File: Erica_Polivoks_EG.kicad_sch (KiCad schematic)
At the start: 92 parts, among them J1 GATE IN, J2 INV EG OUT, J3 Eurorack_Power_10pin_Unshroud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, J4 GATE DELAY OUT, J5 EG OUT, Q1 2N3904, Q2 2N3904, Q3 2N3904, Q4 2N3904, Q5 2N3904, Q6 2N3904, Q7 2N3906, Q8 2N3906, Q9 2N3906, SW1 SW_DPDT_x2, U1 TL074

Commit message: v1.1 ready for final check
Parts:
- R1, R2, R3: footprint Resistor_THT:R_Axial_DIN0207_L6.3mm_D2.5mm_P7.62mm_Horizontal -> Library:R_Axial_DIN0204_L3.6mm_D1.6mm_P7.62mm_Horizontal_Widened; Silkscreen Value (none) -> 200Ω
- R10, R11, R12, R13, R14, R15, R16, R17, R18, R19, R20, R21, R22, R23, R24, R25, R26, R27, R28, R29, R30, R31, R32, R33, R35, R36, R38, R39, R4, R40, R42, R43, R45, R47, R48, R49, R5, R50, R51, R6, R7, R8, R9: footprint Resistor_THT:R_Axial_DIN0207_L6.3mm_D2.5mm_P7.62mm_Horizontal -> Library:R_Axial_DIN0204_L3.6mm_D1.6mm_P7.62mm_Horizontal_Widened
- R34: value NU 39K -> NU 39k; footprint Resistor_THT:R_Axial_DIN0207_L6.3mm_D2.5mm_P7.62mm_Horizontal -> Library:R_Axial_DIN0204_L3.6mm_D1.6mm_P7.62mm_Horizontal_Widened
- R37, R44: footprint Resistor_THT:R_Axial_DIN0207_L6.3mm_D2.5mm_P7.62mm_Horizontal -> Library:R_Axial_DIN0204_L3.6mm_D1.6mm_P7.62mm_Horizontal_Widened; Silkscreen Value ◀470 -> ◀470Ω
- R41: footprint Resistor_THT:R_Axial_DIN0207_L6.3mm_D2.5mm_P7.62mm_Horizontal -> Library:R_Axial_DIN0204_L3.6mm_D1.6mm_P7.62mm_Horizontal_Widened; Silkscreen Value (none) -> 470Ω
- R46: footprint Resistor_THT:R_Axial_DIN0207_L6.3mm_D2.5mm_P7.62mm_Horizontal -> Library:R_Axial_DIN0204_L3.6mm_D1.6mm_P7.62mm_Horizontal_Widened; Silkscreen Value (none) -> 3.3k▼

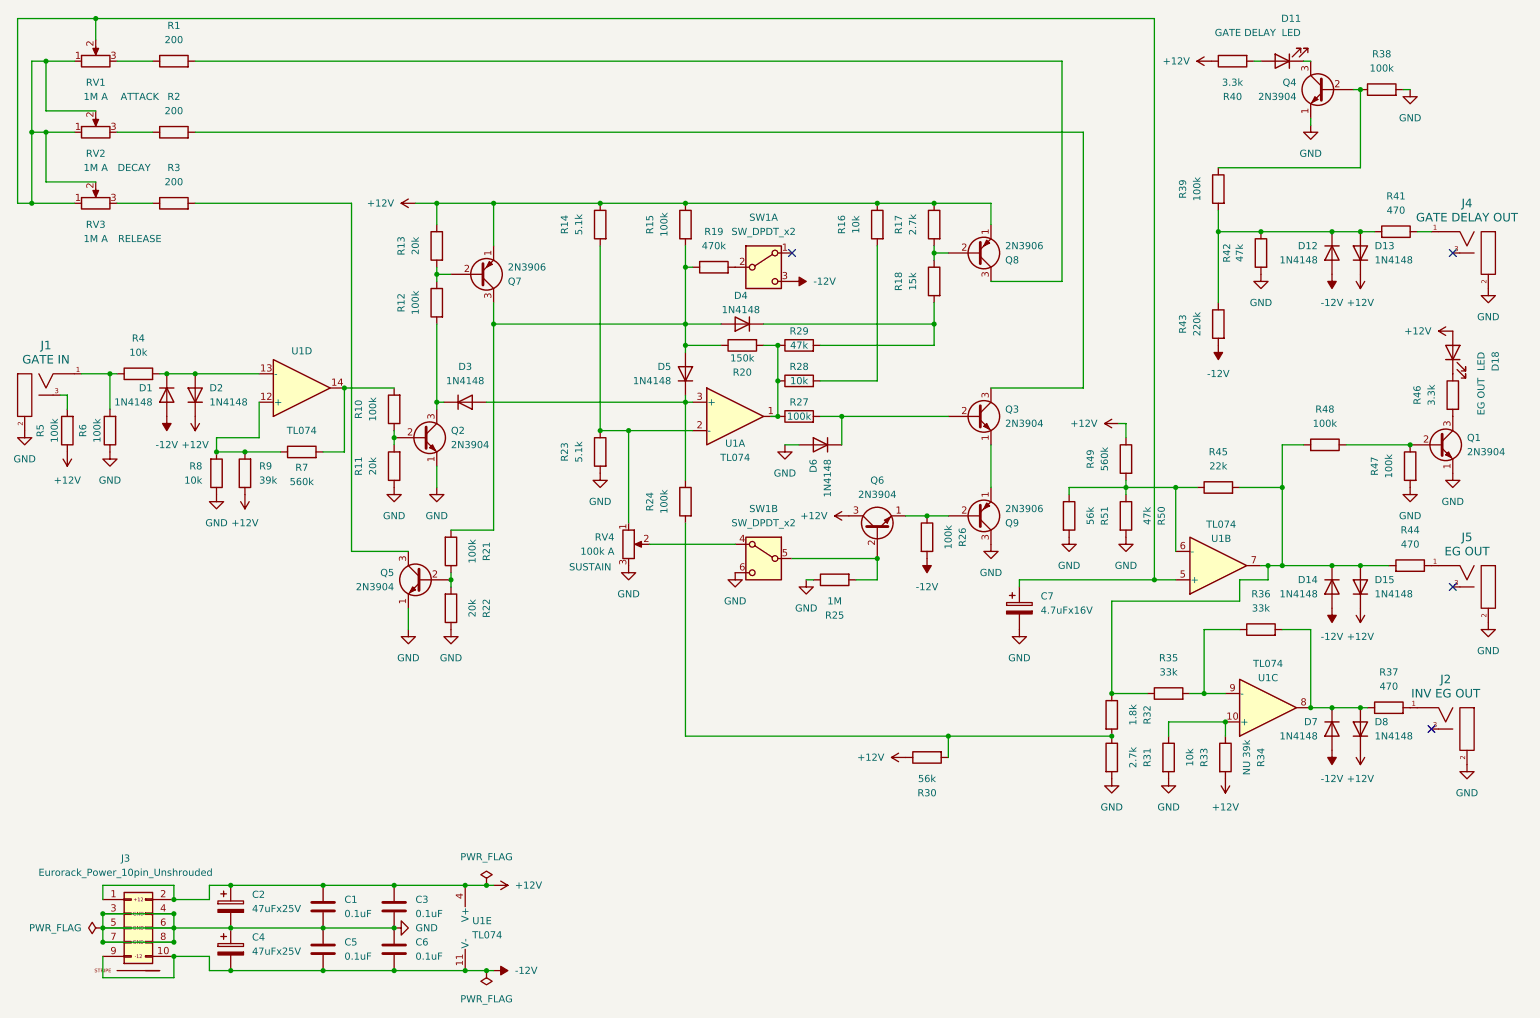
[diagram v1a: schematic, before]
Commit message: rerouting complete and passes DRC
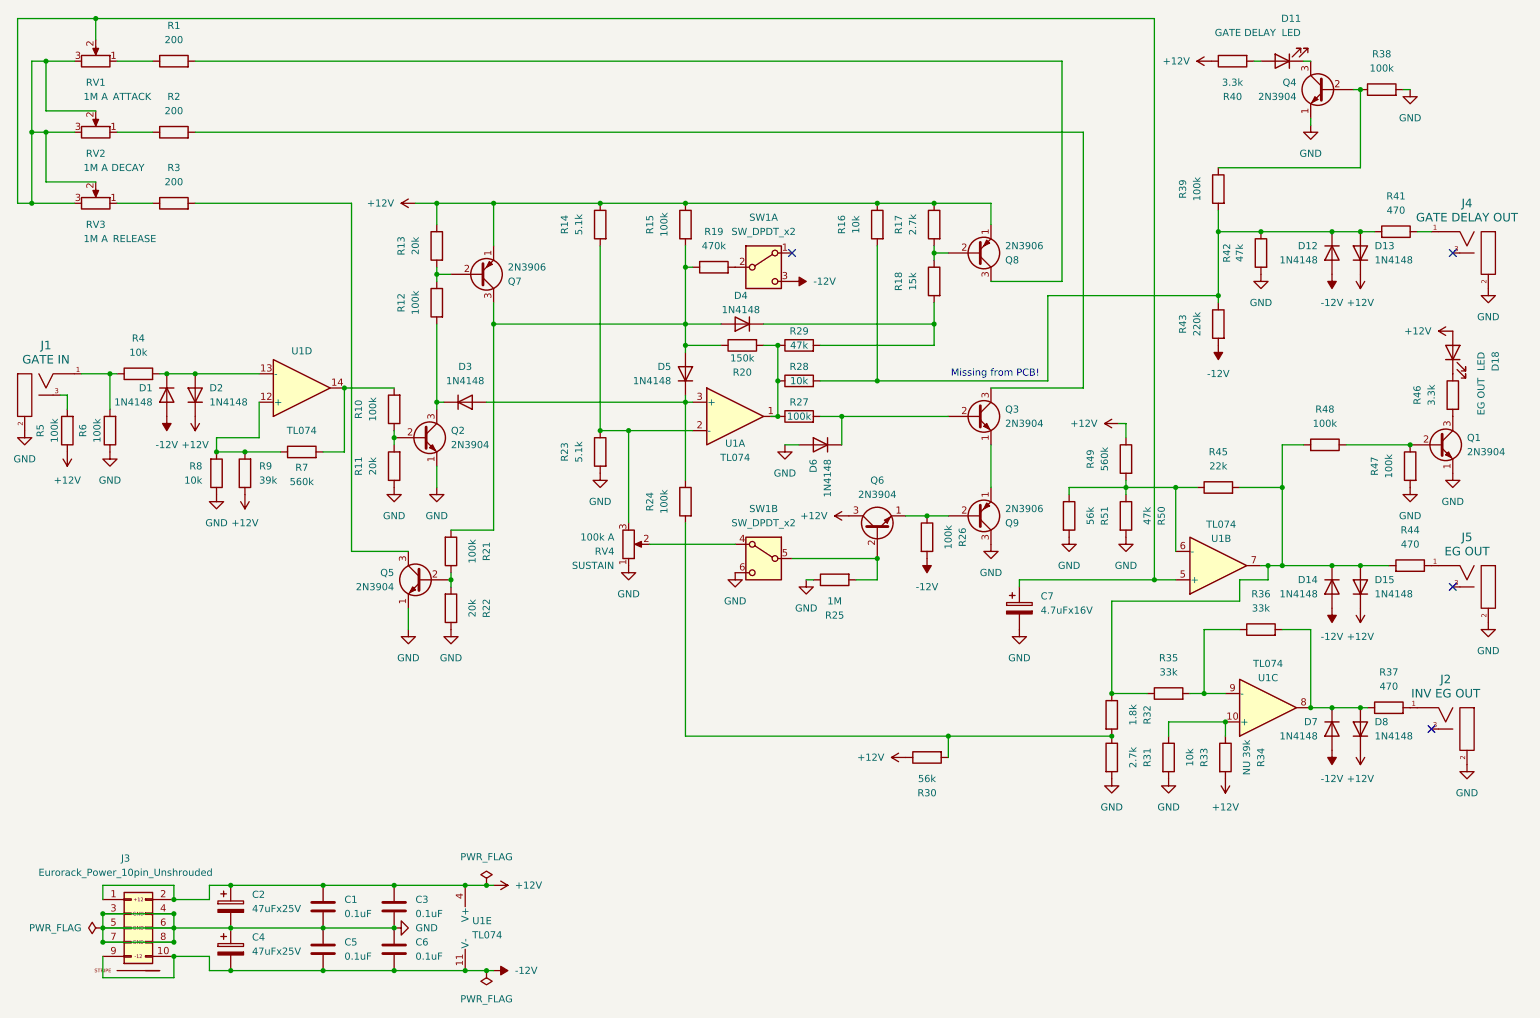
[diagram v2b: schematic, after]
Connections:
- net GND: now also RV4.1; no longer RV4.3
- net at R14.2, R23.1, U1.2 (-): now also RV4.3; no longer RV4.1
- net at C7.1, RV1.2, RV2.2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: now also RV1.3, RV2.3, RV3.3; no longer RV1.1, RV2.1, RV3.1
- net at D12.1 (K), D13.2 (A), R39.2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: now also R16.2, R28.2
- net at R1.1: now also RV1.1; no longer RV1.3
- net at R2.1: now also RV2.1; no longer RV2.3
- net at R3.1: now also RV3.1; no longer RV3.3
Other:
- note added: "Missing from PCB!"
- moved on the sheet: RV1, RV2, RV3
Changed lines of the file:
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@@
 	)
 	(junction
+		(at 229.87 67.31)
+		(diameter 0)
+		(color 0 0 0 0)
+	)
+	(junction
 		(at 255.27 115.57)
 		(diameter 0)
@@
 	)
 	(junction
+		(at 168.91 82.55)
+		(diameter 0)
+		(color 0 0 0 0)
+	)
+	(junction
 		(at 119.38 91.44)
 		(diameter 0)
@@
 	(wire
 		(pts
+			(xy 199.39 67.31) (xy 229.87 67.31)
+		)
+		(stroke
+			(width 0)
+			(type default)
+			(color 255 1 13 1)
+		)
+	)
+	(wire
+		(pts
 			(xy 29.21 17.78) (xy 29.21 21.59)
 		)
@@
 	(wire
 		(pts
-			(xy 229.87 55.88) (xy 229.87 68.58)
+			(xy 229.87 55.88) (xy 229.87 67.31)
 		)
 		(stroke
@@
 	(wire
 		(pts
+			(xy 168.91 82.55) (xy 199.39 82.55)
+		)
+		(stroke
+			(width 0)
+			(type default)
+			(color 255 1 13 1)
+		)
+	)
+	(wire
+		(pts
 			(xy 100.33 50.8) (xy 100.33 58.42)
 		)
@@
 	(wire
 		(pts
+			(xy 229.87 67.31) (xy 229.87 68.58)
+		)
+		(stroke
+			(width 0)
+			(type default)
+		)
+	)
+	(wire
+		(pts
 			(xy 152.4 93.98) (xy 154.94 93.98)
 		)
@@
 	(wire
 		(pts
+			(xy 199.39 82.55) (xy 199.39 67.31)
+		)
+		(stroke
+			(width 0)
+			(type default)
+			(color 255 1 13 1)
+		)
+	)
+	(wire
+		(pts
 			(xy 226.06 101.6) (xy 222.25 101.6)
 		)
@@
 		)
 	)
+	(text "Missing from PCB!"
+		(exclude_from_sim no)
+		(at 189.992 81.28 0)
+		(effects
+			(font
+				(size 1.27 1.27)
+			)
+		)
+	)
 	(symbol
 		(lib_id "Switch:SW_DPDT_x2")
@@
 	(symbol
 		(lib_id "Device:R_Potentiometer")
-		(at 29.21 38.1 90)
+		(at 29.21 38.1 270)
+		(mirror x)
 		(unit 1)
 		(exclude_from_sim no)
@@
 		)
 		(property "Description" "DECAY"
-			(at 36.068 44.45 90)
+			(at 32.004 44.45 90)
 			(effects
 				(font
 					(size 1.27 1.27)
 				)
+				(justify left)
 			)
 		)
@@
 		(lib_id "Device:R_Potentiometer")
 		(at 124.46 111.76 0)
+		(mirror x)
 		(unit 1)
 		(exclude_from_sim no)
@@
 		(dnp no)
 		(property "Reference" "RV4"
-			(at 121.92 110.4899 0)
+			(at 121.92 113.0301 0)
 			(effects
 				(font
@@
 		)
 		(property "Value" "100k A"
-			(at 121.92 113.0299 0)
+			(at 121.92 110.4901 0)
 			(effects
 				(font
@@
 		)
 		(property "Description" "SUSTAIN"
-			(at 117.602 115.824 0)
+			(at 118.11 115.57 0)
 			(effects
 				(font
@@
 	(symbol
 		(lib_id "Device:R_Potentiometer")
-		(at 29.21 25.4 90)
+		(at 29.21 25.4 270)
+		(mirror x)
 		(unit 1)
 		(exclude_from_sim no)
@@
 		)
 		(property "Description" "ATTACK"
-			(at 37.084 31.75 90)
+			(at 32.258 31.75 90)
 			(effects
 				(font
 					(size 1.27 1.27)
 				)
+				(justify left)
 			)
 		)
@@
 	(symbol
 		(lib_id "Device:R_Potentiometer")
-		(at 29.21 50.8 90)
+		(at 29.21 50.8 270)
+		(mirror x)
 		(unit 1)
 		(exclude_from_sim no)
@@
 		)
 		(property "Description" "RELEASE"
-			(at 37.084 57.15 90)
+			(at 32.258 57.15 90)
 			(effects
 				(font
 					(size 1.27 1.27)
 				)
+				(justify left)
 			)
 		)
